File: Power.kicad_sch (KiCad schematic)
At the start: 2 parts, among them J2 Jack-DC

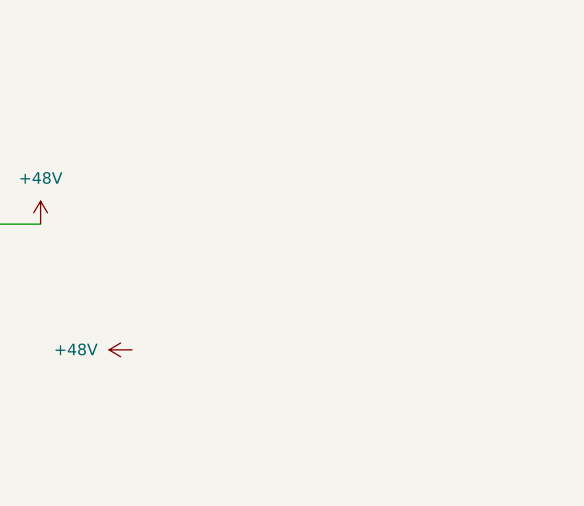
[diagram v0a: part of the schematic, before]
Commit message: added a regulator
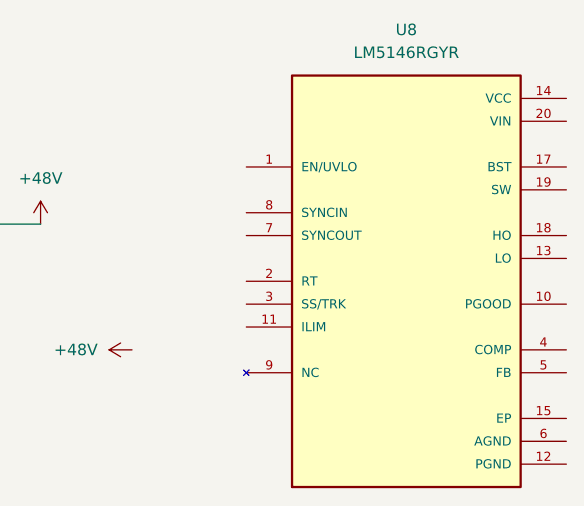
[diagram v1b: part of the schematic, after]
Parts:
- added U8: LM5146RGYR, LM5146RGYR:IC_LM5146RGYR, symbol LM5146RGYR:LM5146RGYR
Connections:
- new net: U8.16 (NC), U8.9 (NC)
- new net EP: U8.15 (EP), U8.21 (EP)

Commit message: power schema properly configured 24v16A and 12v8A
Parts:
- removed U8: LM5146RGYR, LM5146RGYR:IC_LM5146RGYR, symbol LM5146RGYR:LM5146RGYR
- added C155, C175, C190: 47nF, symbol Device:C_Small
- added C156, C157, C158, C159, C160, C165, C168, C169, C172, C173, C176, C181, C183, C184, C187, C188, C192, C196: 4.7uF, symbol Device:C_Small
- added C161, C162, C163, C164, C177, C178, C179, C180, C182, C191, C193, C194, C195, C197: 22uF, symbol Device:C_Small
- added C166, C171: 100pF, symbol Device:C_Small
- added C167, C174, C189: 0.1uF, symbol Device:C_Small
- added C170: 4.7nF, symbol Device:C_Small
- added L15, L16, L17: 6.8uH, symbol Device:L
- added R100, R84, R94: 5m, symbol Device:R_Small
- added R83, R93, R99: 1, symbol Device:R_Small
- added R85, R90: 6.34k, symbol Device:R_Small
- added R86: 29.4K, symbol Device:R_Small
- added R87, R92, R98: 54.9K, symbol Device:R_Small
- added R88: 49.9k, symbol Device:R_Small
- added R89: 10k, symbol Device:R_Small
- added R91: 54.9k, symbol Device:R_Small
- added R95: 290k, symbol Device:R_Small
- added R97: 90.9k, symbol Device:R_Small
- added U10, U8, U9: LM70880RRXR, G-MuzikBox:RRX0029B-MFG, symbol LM70880RRXR:LM70880RRXR
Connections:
- net +48V: now also C157.2, C158.2, C159.2, C160.2, C168.2, C169.2, C172.2, C173.2, C183.2, C184.2, C187.2, C188.2, U10.1 (VIN4), U10.2 (VIN5), U10.27 (VIN1), U10.28 (VIN2), U10.29 (VIN3), U10.3 (VIN6), U10.9 (EN_UVLO), U8.1 (VIN4), U8.2 (VIN5), U8.27 (VIN1), U8.28 (VIN2), U8.29 (VIN3), U8.3 (VIN6), U8.9 (EN_UVLO), U9.1 (VIN4), U9.2 (VIN5), U9.27 (VIN1), U9.28 (VIN2), U9.29 (VIN3), U9.3 (VIN6), U9.9 (EN_UVLO)
- net GNDD: now also C156.1, C157.1, C158.1, C159.1, C160.1, C161.1, C162.1, C163.1, C164.1, C165.2, C166.2, C168.1, C169.1, C172.1, C173.1, C176.1, C177.1, C178.1, C179.1, C180.1, C181.2, C182.1, C183.1, C184.1, C187.1, C188.1, C191.1, C192.1, C193.1, C194.1, C195.1, C196.2, C197.1, U10.23 (PGND1), U10.24 (PGND2), U10.25 (PGND3), U10.26 (PGND4), U10.30 (PGND), U8.23 (PGND1), U8.24 (PGND2), U8.25 (PGND3), U8.26 (PGND4), U8.30 (PGND), U9.23 (PGND1), U9.24 (PGND2), U9.25 (PGND3), U9.26 (PGND4), U9.30 (PGND)
- new net: C190.2, R99.1
- new net: L17.1, R99.2, U10.20 (SW1), U10.21 (SW2), U10.22 (SW3), U10.5 (SW4)
- new net: L17.2, R100.1, U10.11 (ISNS+)
- new net: C192.2, U10.19 (VCC)
- new net: R92.2, U9.14 (RT)
- new net: R91.2, U9.13 (CONFIG)
- new net: L16.1, R93.2, U9.20 (SW1), U9.21 (SW2), U9.22 (SW3), U9.5 (SW4)
- new net: L16.2, R94.1, U9.11 (ISNS+)
- new net: L15.2, R84.1, U8.11 (ISNS+)
- new net: C174.2, U9.18 (VDDA)
- new net: R97.2, U10.13 (CONFIG)
- new net: C165.1, R85.1
- new net: C166.1, R85.2, U8.15 (EXTCOMP)
- new net: R86.2, U8.13 (CONFIG)
- new net: C176.2, U9.19 (VCC)
- new net: R87.2, U8.14 (RT)
- new net: R89.2, R95.1, U9.16 (FB)
- new net: R98.2, U10.14 (RT)
- new net: C171.1, R90.2, U10.15 (EXTCOMP), U9.15 (EXTCOMP)
- new net: C189.2, U10.18 (VDDA)
- new net: C190.1, U10.4 (CBOOT)
- new net: U10.8 (PFM_SYNCIN), U9.7 (PG_SYNCOUT)
- new net: L15.1, R83.2, U8.20 (SW1), U8.21 (SW2), U8.22 (SW3), U8.5 (SW4)
- new net: C170.1, R90.1
- new net: C155.2, R83.1
- new net: C167.2, R88.1, U8.18 (VDDA)
- new net: C175.1, U9.4 (CBOOT)
- new net: R88.2, U8.16 (FB)
- new net: C175.2, R93.1
- new net: C155.1, U8.4 (CBOOT)
- new net: C156.2, U8.19 (VCC)
- new net +12V: C161.2, C162.2, C163.2, C164.2, R84.2, U8.12 (VOUT), U8.6 (BIAS)
- new net +24V: C177.2, C178.2, C179.2, C180.2, C181.1, C182.2, C191.2, C193.2, C194.2, C195.2, C196.1, C197.2, R100.2, R94.2, R95.2, U10.12 (VOUT), U10.6 (BIAS), U9.12 (VOUT), U9.6 (BIAS)
- new net 12V_power-good signal: U8.7 (PG_SYNCOUT)
- new net 24V_power-good signal: U10.7 (PG_SYNCOUT)
- new net GNDA: C167.1, C170.2, C171.2, C174.1, C189.1, R86.1, R87.1, R89.1, R91.1, R92.1, R97.1, R98.1, U10.16 (FB), U10.17 (AGND), U8.17 (AGND), U8.8 (PFM_SYNCIN), U9.17 (AGND), U9.8 (PFM_SYNCIN)
- no-connect marks 0 -> 3
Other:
- moved on the sheet: F1, J2
